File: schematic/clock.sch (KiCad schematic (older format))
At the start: 1 part

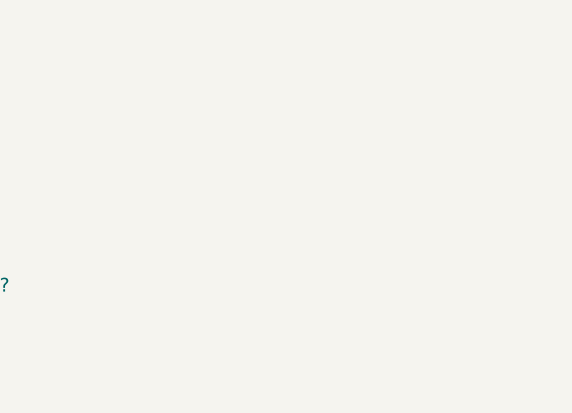
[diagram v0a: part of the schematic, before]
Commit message: sbc schematic update. This version appears to boot
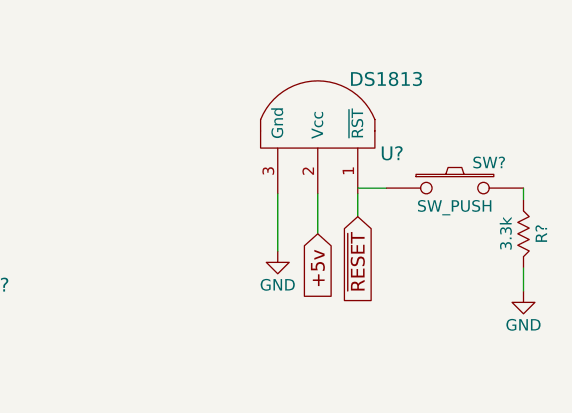
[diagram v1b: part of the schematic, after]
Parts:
- added R?: 3.3k, symbol Rsqig
- added SW?: SW_PUSH, symbol SW_PUSH
- added U?: DS1813, symbol DS1813
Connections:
- net labels added: ~RESET~
- wire segments 3 -> 9
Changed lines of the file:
@@
 	1625 2475 1625 2400
 NoConn ~ 1625 3325
+$Comp
+L DS1813 U?
+U 1 1 581AC38B
+P 3700 2550
+F 0 "U?" H 4000 2550 60  0000 C CNN
+F 1 "DS1813" H 3975 2875 60  0000 C CNN
+F 2 "" H 3975 2875 60  0000 C CNN
+F 3 "" H 3975 2875 60  0000 C CNN
+	1    3700 2550
+	1    0    0    -1
+$EndComp
+Text GLabel 3850 2825 3    60   Input ~ 0
+~RESET~
+$Comp
+L GND #PWR?
+U 1 1 581AC43C
+P 3500 2975
+F 0 "#PWR?" H 3500 2725 50  0001 C CNN
+F 1 "GND" H 3500 2825 50  0000 C CNN
+F 2 "" H 3500 2975 50  0000 C CNN
+F 3 "" H 3500 2975 50  0000 C CNN
+	1    3500 2975
+	1    0    0    -1
+$EndComp
+Text GLabel 3675 2900 3    60   Input ~ 0
++5v
+Wire Wire Line
+	3500 2725 3500 2975
+Wire Wire Line
+	3675 2725 3675 2900
+Wire Wire Line
+	3850 2725 3850 2825
+$Comp
+L SW_PUSH SW?
+U 1 1 581AC48C
+P 4275 2700
+F 0 "SW?" H 4425 2810 50  0000 C CNN
+F 1 "SW_PUSH" H 4275 2620 50  0000 C CNN
+F 2 "" H 4275 2700 50  0000 C CNN
+F 3 "" H 4275 2700 50  0000 C CNN
+	1    4275 2700
+	1    0    0    -1
+$EndComp
+Wire Wire Line
+	3850 2700 3975 2700
+$Comp
+L Rsqig R?
+U 1 1 581AC631
+P 4575 2900
+F 0 "R?" V 4655 2900 50  0000 C CNN
+F 1 "3.3k" V 4500 2900 50  0000 C CNN
+F 2 "" V 4505 2900 50  0000 C CNN
+F 3 "" H 4575 2900 50  0000 C CNN
+	1    4575 2900
+	1    0    0    -1
+$EndComp
+$Comp
+L GND #PWR?
+U 1 1 581AC694
+P 4575 3150
+F 0 "#PWR?" H 4575 2900 50  0001 C CNN
+F 1 "GND" H 4575 3000 50  0000 C CNN
+F 2 "" H 4575 3150 50  0000 C CNN
+F 3 "" H 4575 3150 50  0000 C CNN
+	1    4575 3150
+	1    0    0    -1
+$EndComp
+Wire Wire Line
+	4575 3150 4575 3050
+Wire Wire Line
+	4575 2750 4575 2700
 $EndSCHEMATC

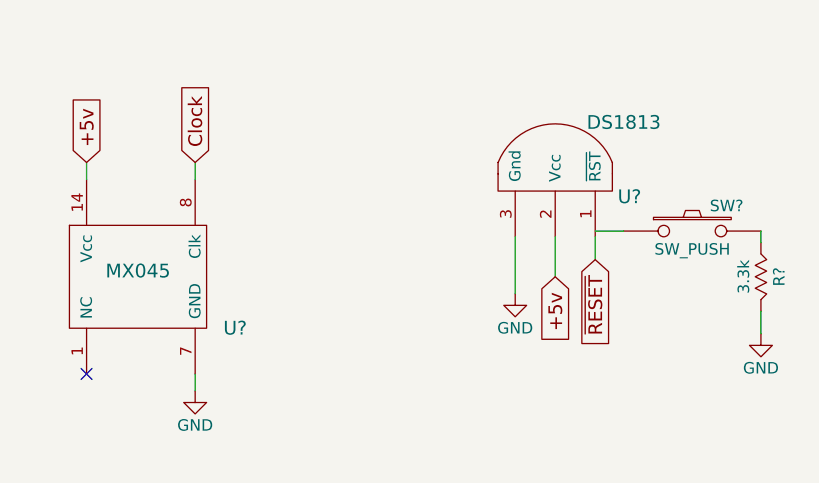
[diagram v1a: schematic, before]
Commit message: sbc added FRAM to schematic
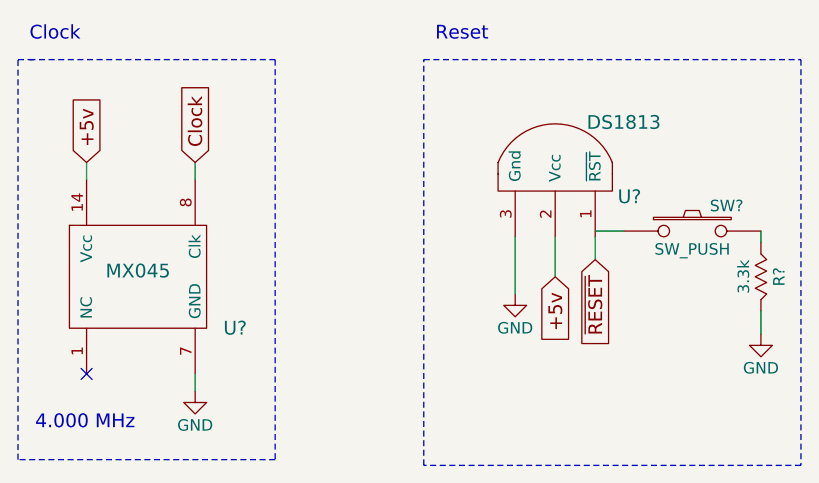
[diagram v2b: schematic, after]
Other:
- note added: "4.000 MHz"
- note added: "Clock"
- note added: "Reset"
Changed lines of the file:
@@
 $Descr A4 11693 8268
 encoding utf-8
-Sheet 2 3
+Sheet 2 4
 Title ""
 Date ""
@@
 Wire Wire Line
 	4575 2750 4575 2700
+Wire Notes Line
+	1375 1950 2450 1950
+Wire Notes Line
+	2450 1950 2450 3700
+Wire Notes Line
+	2450 3700 1325 3700
+Wire Notes Line
+	1325 3700 1325 1950
+Wire Notes Line
+	1325 1950 1400 1950
+Wire Notes Line
+	3100 1950 4750 1950
+Wire Notes Line
+	4750 1950 4750 3725
+Wire Notes Line
+	4750 3725 3100 3725
+Wire Notes Line
+	3100 3725 3100 1950
+Text Notes 1400 3575 0    60   ~ 0
+4.000 MHz
+Text Notes 3150 1875 0    60   ~ 0
+Reset
+Text Notes 1375 1875 0    60   ~ 0
+Clock
 $EndSCHEMATC

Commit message: Updated SBC schematic
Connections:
- wire segments 9 -> 12
- no-connect marks 1 -> 0
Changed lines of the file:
@@
 Wire Wire Line
 	1625 2475 1625 2400
-NoConn ~ 1625 3325
 $Comp
 L DS1813 U?
@@
 Text Notes 1375 1875 0    60   ~ 0
 Clock
+Wire Wire Line
+	1625 2450 1450 2450
+Wire Wire Line
+	1450 2450 1450 3325
+Wire Wire Line
+	1450 3325 1625 3325
+Connection ~ 1625 2450
 $EndSCHEMATC

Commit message: SBC Schematic final
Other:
- note added: "December 10th, 2016"
- note added: "Micheal Burin - ECEN 5613"
- note added: "SBC - Clock and Reset"
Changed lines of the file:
@@
 	1450 3325 1625 3325
 Connection ~ 1625 2450
+Text Notes 7050 6700 0    60   ~ 0
+Micheal Burin  - ECEN 5613
+Text Notes 7350 7500 0    60   ~ 0
+SBC - Clock and Reset
+Text Notes 8150 7650 0    60   ~ 0
+December 10th, 2016
 $EndSCHEMATC
